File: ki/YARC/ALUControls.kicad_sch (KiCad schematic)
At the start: 12 parts, among them U107 74HC00, U123 74LS32, U124 74LS08, U125 74LS08, U126 74LS00, U127 74LS74, U129 74LS574, U130 74LS157, U131 74LS245, U93 74LS32

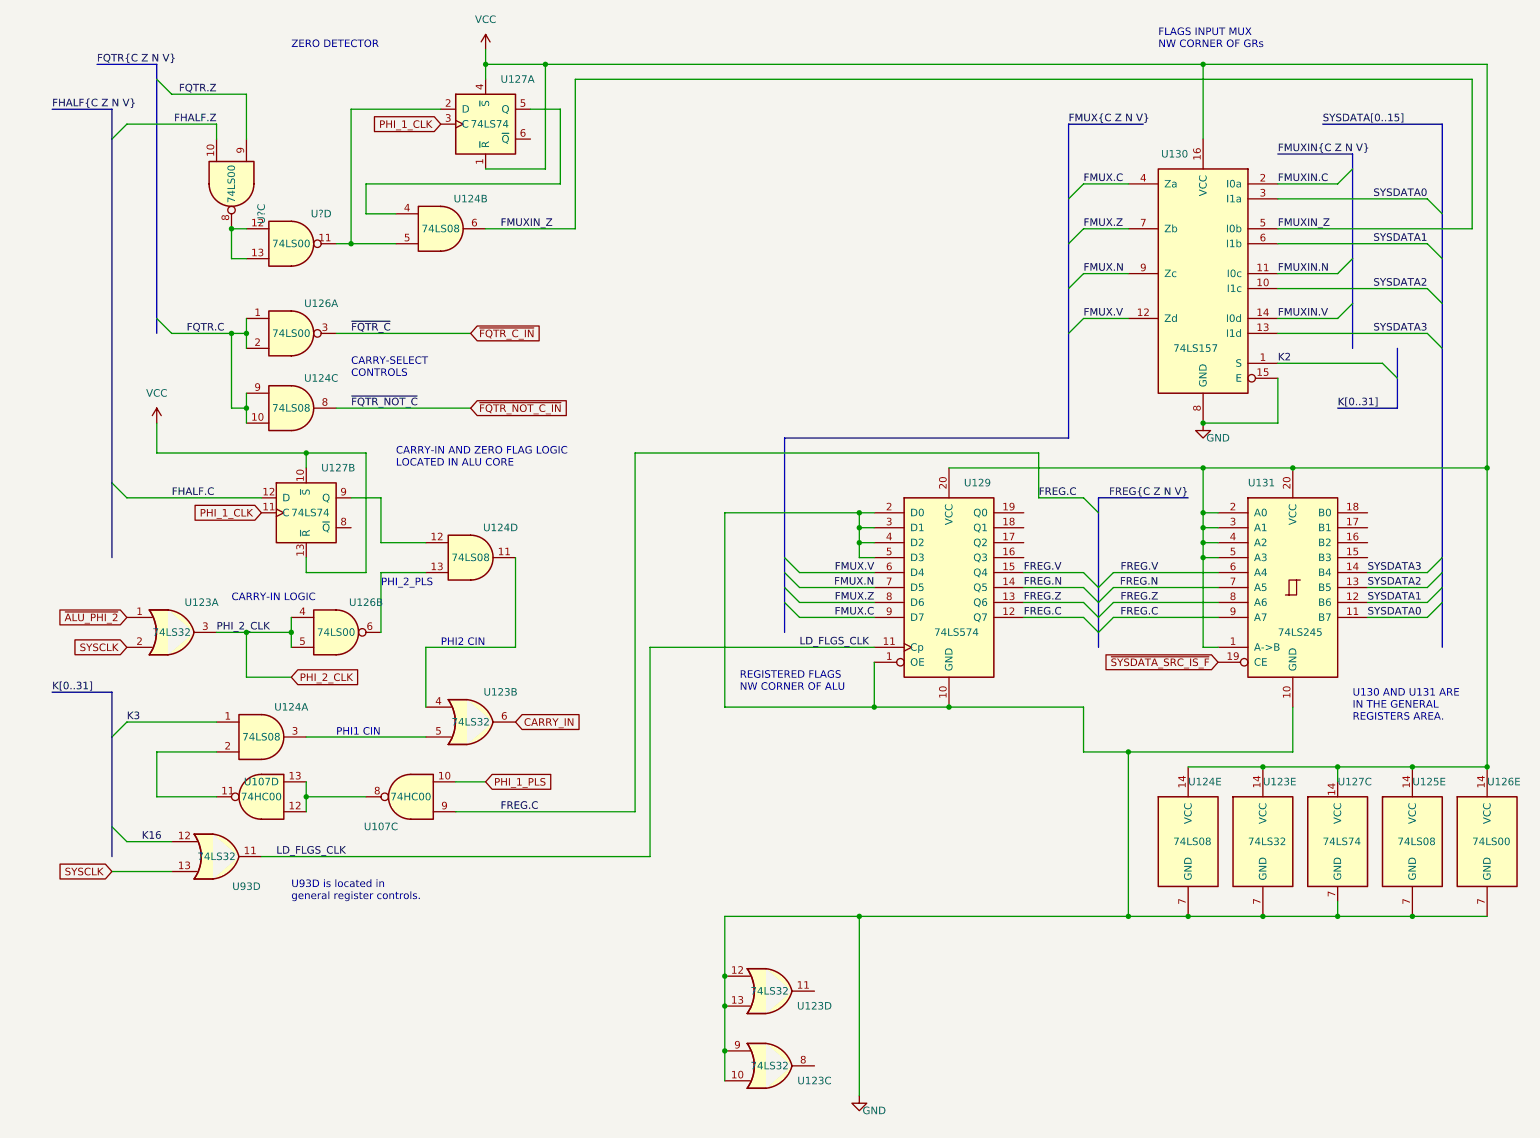
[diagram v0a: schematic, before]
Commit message: Yet more cleanup on ALU and flags design
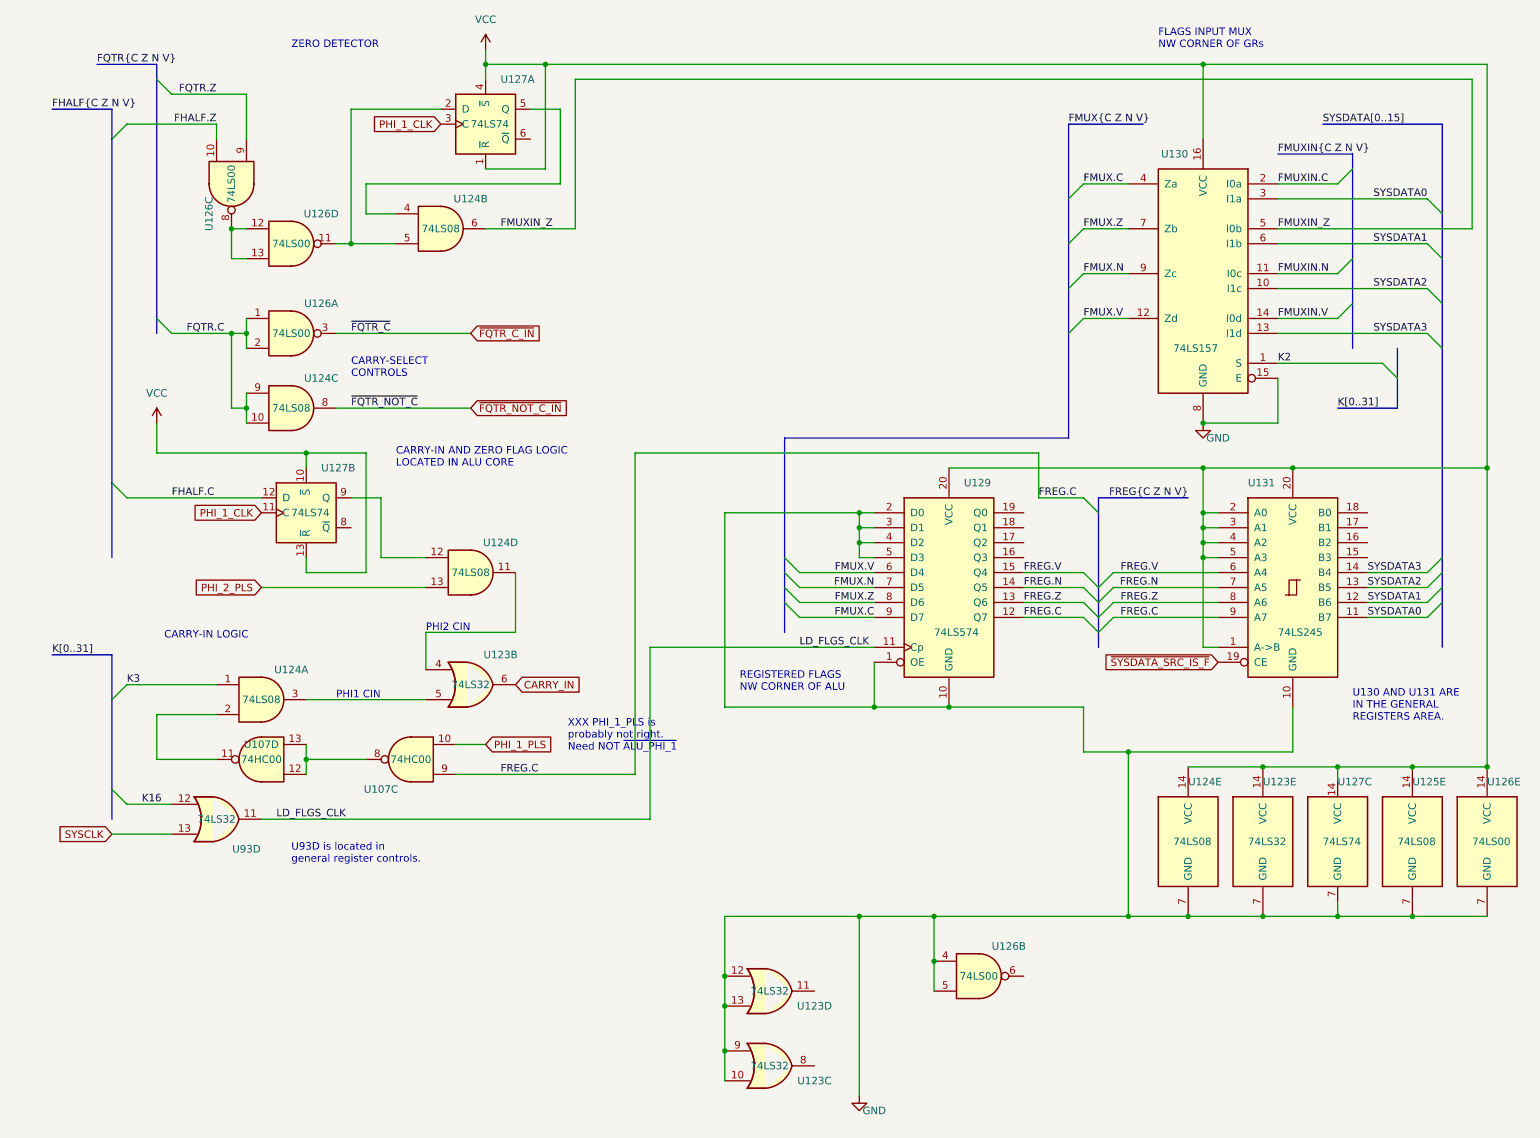
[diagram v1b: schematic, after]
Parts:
- removed unit 1 of U123
- gave numbers to parts that had none: 1
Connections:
- net PHI_2_CLK is gone; now on net GND: U126.4, U126.5
- net at U126.6: no longer U124.13
- new net PHI_2_PLS: U124.13
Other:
- note added: "XXX PHI_1_PLS is probably not right. Need NOT ~{ALU_PHI_1}"
- note removed: "PHI_2_PLS"
- moved on the sheet: U107C, U107D, U123B, U124A, U124D, U93D

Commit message: Fix schematic error in <= gate. Cleanup signal naming. Fix subtle issue with carry in signal.
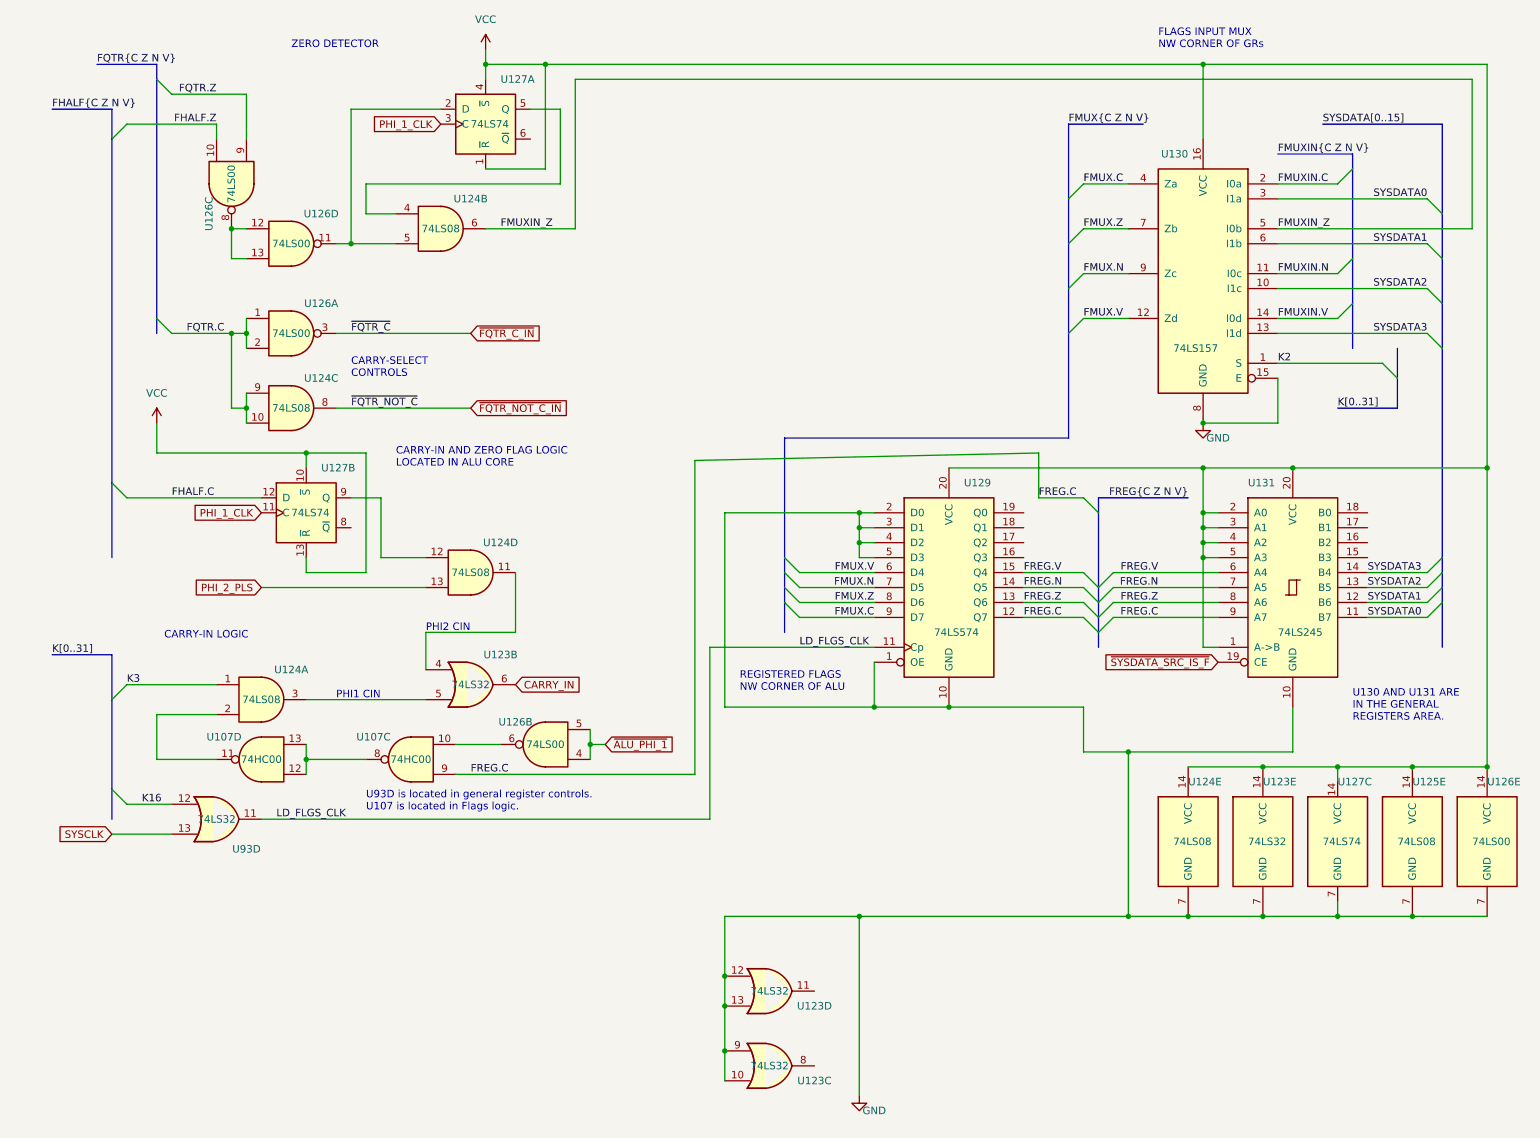
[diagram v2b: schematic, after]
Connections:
- net PHI_1_PLS is gone; now on an unnamed net: U107.10
- net GND: no longer U126.4, U126.5
- new net ~{ALU_PHI_1}: U126.4, U126.5
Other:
- note added: "U93D is located in general register controls. U107 is located in Flags logic."
- note removed: "U93D is located in general register controls."
- note removed: "XXX PHI_1_PLS is probably not right. Need NOT ~{ALU_PHI_1}"
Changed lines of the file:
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@@
   (junction (at 210.82 101.6) (diameter 0) (color 0 0 0 0)
   )
+  (junction (at 106.68 138.43) (diameter 0) (color 0 0 0 0)
+  )
   (junction (at 220.98 167.64) (diameter 0) (color 0 0 0 0)
   )
@@
   (junction (at 129.54 190.5) (diameter 0) (color 0 0 0 0)
   )
-  (junction (at 165.1 175.26) (diameter 0) (color 0 0 0 0)
-  )
   (junction (at 210.82 83.82) (diameter 0) (color 0 0 0 0)
   )
@@
   (junction (at 48.26 68.58) (diameter 0) (color 0 0 0 0)
   )
-  (junction (at 165.1 167.64) (diameter 0) (color 0 0 0 0)
-  )
   (junction (at 226.06 91.44) (diameter 0) (color 0 0 0 0)
   )
@@
     (stroke (width 0) (type default) (color 0 0 0 0))
   )
-  (wire (pts (xy 50.8 151.13) (xy 116.84 151.13))
+  (wire (pts (xy 50.8 151.13) (xy 127 151.13))
     (stroke (width 0) (type default) (color 0 0 0 0))
   )
@@
     (stroke (width 0) (type default) (color 0 0 0 0))
   )
-  (wire (pts (xy 83.82 138.43) (xy 88.9 138.43))
-    (stroke (width 0) (type default) (color 0 0 0 0))
-  )
   (bus (pts (xy 231.14 33.02) (xy 251.46 33.02))
     (stroke (width 0) (type default) (color 0 0 0 0))
@@
     (stroke (width 0) (type default) (color 0 0 0 0))
   )
+  (wire (pts (xy 91.44 138.43) (xy 83.82 138.43))
+    (stroke (width 0) (type default) (color 0 0 0 0))
+  )
+  (wire (pts (xy 109.22 138.43) (xy 106.68 138.43))
+    (stroke (width 0) (type default) (color 0 0 0 0))
+  )
   (wire (pts (xy 58.42 109.22) (xy 58.42 106.68))
     (stroke (width 0) (type default) (color 0 0 0 0))
@@
     (stroke (width 0) (type default) (color 0 0 0 0))
   )
+  (wire (pts (xy 127 151.13) (xy 127 121.92))
+    (stroke (width 0) (type default) (color 0 0 0 0))
+  )
   (bus (pts (xy 22.86 22.86) (xy 33.02 22.86))
     (stroke (width 0) (type default) (color 0 0 0 0))
   )
+  (wire (pts (xy 106.68 135.89) (xy 106.68 138.43))
+    (stroke (width 0) (type default) (color 0 0 0 0))
+  )
   (bus (pts (xy 25.4 123.19) (xy 25.4 130.81))
     (stroke (width 0) (type default) (color 0 0 0 0))
@@
     (stroke (width 0) (type default) (color 0 0 0 0))
   )
-  (wire (pts (xy 165.1 180.34) (xy 165.1 175.26))
-    (stroke (width 0) (type default) (color 0 0 0 0))
-  )
   (bus (pts (xy 187.96 53.34) (xy 187.96 60.96))
     (stroke (width 0) (type default) (color 0 0 0 0))
@@
     (stroke (width 0) (type default) (color 0 0 0 0))
   )
-  (wire (pts (xy 116.84 121.92) (xy 154.94 121.92))
+  (wire (pts (xy 127 121.92) (xy 154.94 121.92))
     (stroke (width 0) (type default) (color 0 0 0 0))
   )
@@
     (stroke (width 0) (type default) (color 0 0 0 0))
   )
-  (wire (pts (xy 114.3 88.9) (xy 114.3 143.51))
+  (wire (pts (xy 124.46 90.17) (xy 124.46 143.51))
     (stroke (width 0) (type default) (color 0 0 0 0))
   )
@@
     (stroke (width 0) (type default) (color 0 0 0 0))
   )
-  (wire (pts (xy 165.1 167.64) (xy 198.12 167.64))
+  (wire (pts (xy 152.4 167.64) (xy 198.12 167.64))
     (stroke (width 0) (type default) (color 0 0 0 0))
   )
@@
     (stroke (width 0) (type default) (color 0 0 0 0))
   )
-  (wire (pts (xy 83.82 143.51) (xy 114.3 143.51))
+  (wire (pts (xy 83.82 143.51) (xy 124.46 143.51))
     (stroke (width 0) (type default) (color 0 0 0 0))
   )
@@
     (stroke (width 0) (type default) (color 0 0 0 0))
   )
-  (wire (pts (xy 152.4 167.64) (xy 165.1 167.64))
+  (wire (pts (xy 106.68 138.43) (xy 106.68 140.97))
     (stroke (width 0) (type default) (color 0 0 0 0))
   )
@@
     (stroke (width 0) (type default) (color 0 0 0 0))
   )
-  (wire (pts (xy 165.1 175.26) (xy 165.1 167.64))
-    (stroke (width 0) (type default) (color 0 0 0 0))
-  )
   (wire (pts (xy 45.72 55.88) (xy 45.72 50.8))
     (stroke (width 0) (type default) (color 0 0 0 0))
@@
     (stroke (width 0) (type default) (color 0 0 0 0))
   )
-  (wire (pts (xy 116.84 151.13) (xy 116.84 121.92))
-    (stroke (width 0) (type default) (color 0 0 0 0))
-  )
   (wire (pts (xy 223.52 76.2) (xy 223.52 83.82))
     (stroke (width 0) (type default) (color 0 0 0 0))
@@
     (stroke (width 0) (type default) (color 0 0 0 0))
   )
-  (wire (pts (xy 114.3 88.9) (xy 182.88 88.9))
+  (wire (pts (xy 124.46 90.17) (xy 182.88 88.9))
     (stroke (width 0) (type default) (color 0 0 0 0))
   )
@@
     (effects (font (size 1.27 1.27)) (justify left bottom))
   )
-  (text "XXX PHI_1_PLS is\nprobably not right.\nNeed NOT ~{ALU_PHI_1}"
-    (at 102.87 139.7 0)
-    (effects (font (size 1.27 1.27)) (justify left bottom))
-  )
-  (text "U93D is located in\ngeneral register controls." (at 55.88 158.75 0)
+  (text "U93D is located in general register controls.\nU107 is located in Flags logic."
+    (at 68.58 149.86 0)
     (effects (font (size 1.27 1.27)) (justify left bottom))
   )
@@
     (effects (font (size 1.27 1.27)) (justify left bottom))
   )
-  (label "FREG.C" (at 91.44 143.51 0)
+  (label "FREG.C" (at 86.36 143.51 0)
     (effects (font (size 1.27 1.27)) (justify left bottom))
   )
@@
   (label "FMUXIN_Z" (at 91.44 50.8 0)
     (effects (font (size 1.27 1.27)) (justify left bottom))
+  )
+  (global_label "~{ALU_PHI_1}" (shape input) (at 109.22 138.43 0) (fields_autoplaced)
+    (effects (font (size 1.27 1.27)) (justify left))
+    (property "Intersheet References" "${INTERSHEET_REFS}" (id 0) (at 121.4302 138.5094 0)
+      (effects (font (size 1.27 1.27)) (justify left) hide)
+    )
   )
   (global_label "SYSCLK" (shape input) (at 25.4 153.67 180) (fields_autoplaced)
@@
     (property "Intersheet References" "${INTERSHEET_REFS}" (id 0) (at 15.9112 153.5906 0)
       (effects (font (size 1.27 1.27)) (justify right) hide)
-    )
-  )
-  (global_label "PHI_1_PLS" (shape input) (at 88.9 138.43 0) (fields_autoplaced)
-    (effects (font (size 1.27 1.27)) (justify left))
-    (property "Intersheet References" "${INTERSHEET_REFS}" (id 0) (at 101.1707 138.3506 0)
-      (effects (font (size 1.27 1.27)) (justify left) hide)
     )
   )
@@
     (pin "13")
   )
+  (symbol (lib_id "74xx:74LS00") (at 99.06 138.43 180) (unit 2)
+    (in_bom yes) (on_board yes)
+    (property "Reference" "U126" (id 0) (at 93.98 134.62 0))
+    (property "Value" "74LS00" (id 1) (at 99.06 138.43 0))
+    (property "Footprint" "" (id 2) (at 99.06 138.43 0)
+      (effects (font (size 1.27 1.27)) hide)
+    )
+    (property "Datasheet" "http://www.ti.com/lit/gpn/sn74ls00" (id 3) (at 99.06 138.43 0)
+      (effects (font (size 1.27 1.27)) hide)
+    )
+    (pin "4")
+    (pin "5")
+    (pin "6")
+  )
   (symbol (lib_id "74xx:74LS74") (at 58.42 99.06 0) (unit 2)
     (in_bom yes) (on_board yes)
@@
   (symbol (lib_id "74xx:74HC00") (at 76.2 140.97 180) (unit 3)
     (in_bom yes) (on_board yes)
-    (property "Reference" "U107" (id 0) (at 71.12 146.05 0))
+    (property "Reference" "U107" (id 0) (at 69.85 137.16 0))
     (property "Value" "74HC00" (id 1) (at 76.2 140.97 0))
     (property "Footprint" "" (id 2) (at 76.2 140.97 0)
@@
   (symbol (lib_id "74xx:74HC00") (at 50.8 140.97 180) (unit 4)
     (in_bom yes) (on_board yes)
-    (property "Reference" "U107" (id 0) (at 50.8 138.43 0))
+    (property "Reference" "U107" (id 0) (at 44.45 137.16 0))
     (property "Value" "74HC00" (id 1) (at 50.8 140.97 0))
     (property "Footprint" "" (id 2) (at 50.8 140.97 0)
@@
     (pin "13")
   )
-  (symbol (lib_id "74xx:74LS00") (at 172.72 177.8 0) (unit 2)
-    (in_bom yes) (on_board yes)
-    (property "Reference" "U126" (id 0) (at 177.8 172.72 0))
-    (property "Value" "74LS00" (id 1) (at 172.72 177.8 0))
-    (property "Footprint" "" (id 2) (at 172.72 177.8 0)
-      (effects (font (size 1.27 1.27)) hide)
-    )
-    (property "Datasheet" "http://www.ti.com/lit/gpn/sn74ls00" (id 3) (at 172.72 177.8 0)
-      (effects (font (size 1.27 1.27)) hide)
-    )
-    (pin "4")
-    (pin "5")
-    (pin "6")
-  )
   (symbol (lib_id "74xx:74LS08") (at 50.8 130.81 0) (unit 1)

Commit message: Ongoing corrections. Document the Nano's sysbus enable control for the first time.
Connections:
- net PHI_2_PLS renamed ~{ALU_PHI_2}
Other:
- note added: "INVERTER NEEDED HERE"
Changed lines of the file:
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@@
+    (effects (font (size 1.27 1.27)) (justify left bottom))
+  )
+  (text "INVERTER NEEDED HERE" (at 53.34 114.3 0)
     (effects (font (size 1.27 1.27)) (justify left bottom))
   )
@@
     )
   )
-  (global_label "PHI_2_PLS" (shape input) (at 50.8 111.76 180) (fields_autoplaced)
+  (global_label "~{ALU_PHI_2}" (shape input) (at 50.8 111.76 180) (fields_autoplaced)
     (effects (font (size 1.27 1.27)) (justify right))
-    (property "Intersheet References" "${INTERSHEET_REFS}" (id 0) (at 38.5293 111.8394 0)
+    (property "Intersheet References" "${INTERSHEET_REFS}" (id 0) (at 38.5898 111.6806 0)
       (effects (font (size 1.27 1.27)) (justify right) hide)
     )
